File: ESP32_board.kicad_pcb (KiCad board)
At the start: 4 copper layers, 71 parts, among them J4 Conn_01x04_Pin, J5 Conn_01x05_Pin, Q2 BC817, Q3 BC817, U1 MCP73871, U5 USBLC6-2SC6

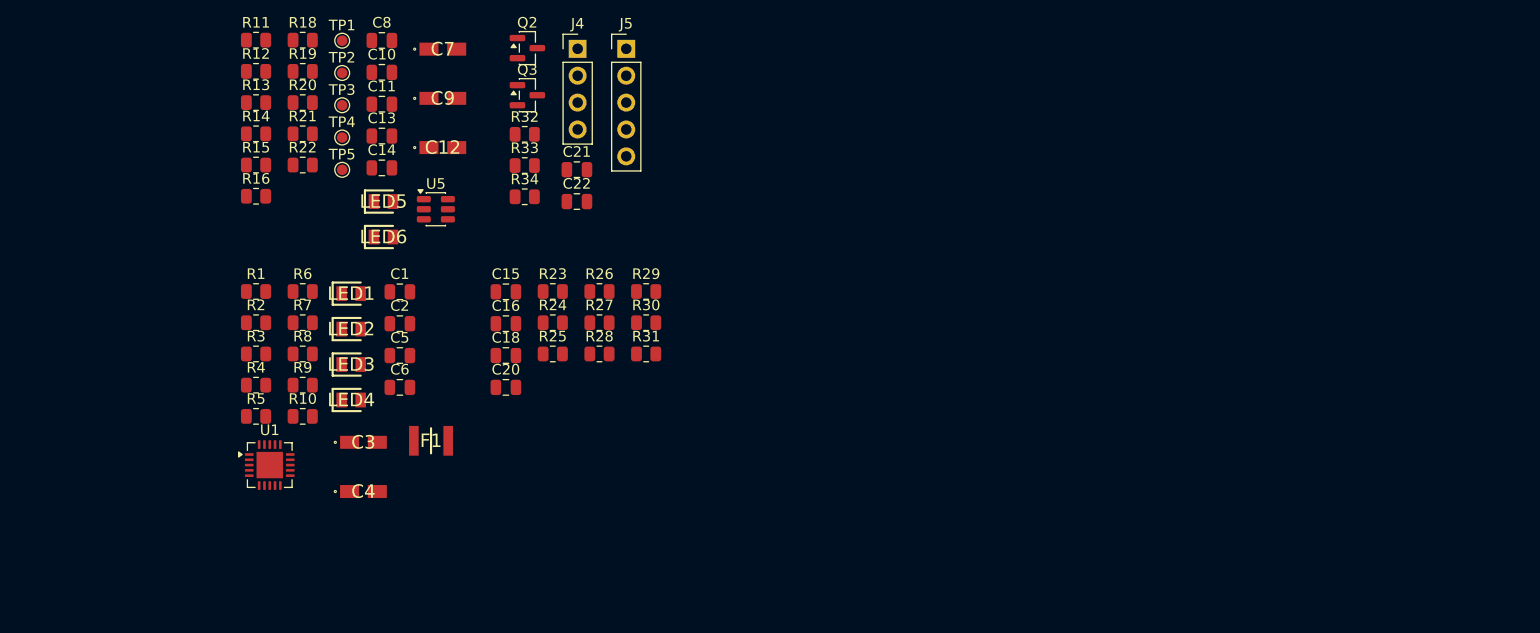
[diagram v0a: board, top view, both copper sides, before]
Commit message: imported all footprints into layout
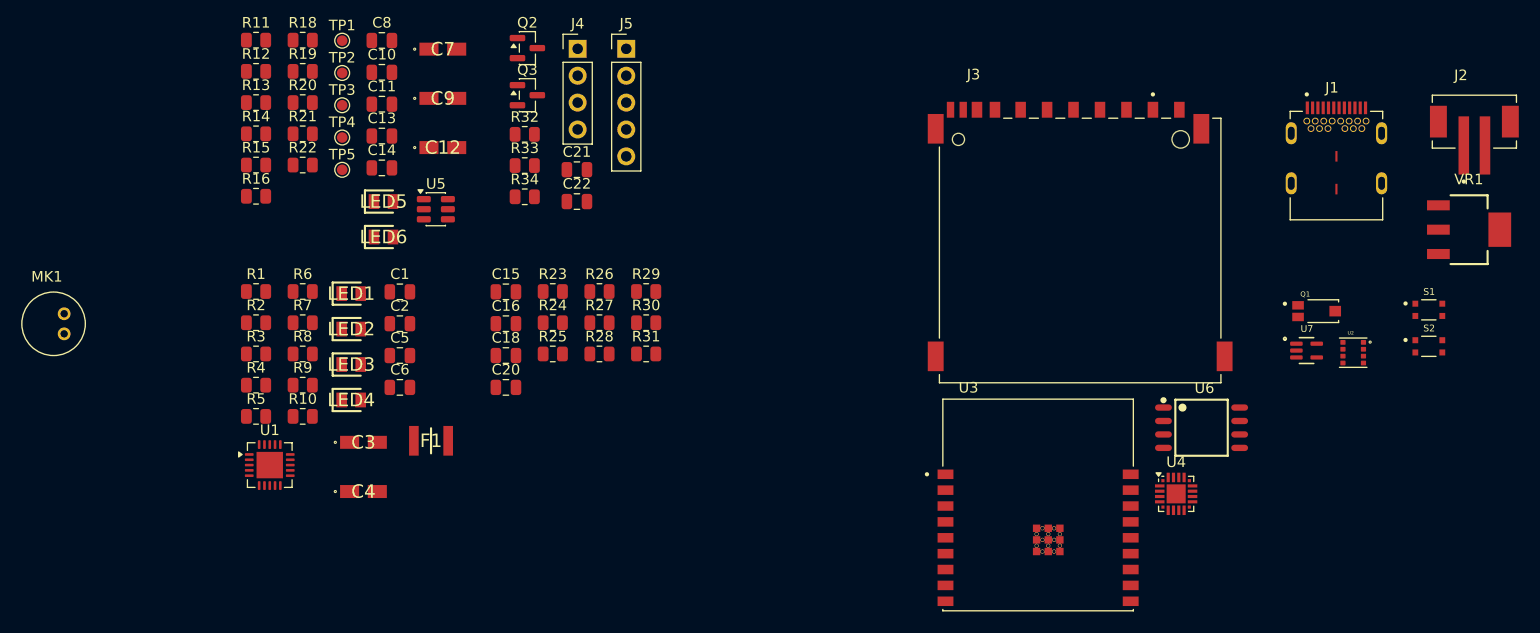
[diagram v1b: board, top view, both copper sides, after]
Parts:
- added J1: SS-52400-002, ESP32_project_Footprints:BELFUSE_SS-52400-002, F.Cu at (221.7, 59.4)
- added J2: B2B-PH-SM4-TB, ESP32_project_Footprints:JST_B2B-PH-SM4-TB, F.Cu at (234.7, 53.6)
- added J3: GSD090012SEU, ESP32_project_Footprints:AMPHENOL_GSD090012SEU, F.Cu at (197.5, 65.8)
- added MK1: CMC-5042PF-AC, ESP32_project_Footprints:CUI_CMC-5042PF-AC, F.Cu at (100.5, 72.7)
- added Q1: TEMT6000X01, ESP32_project_Footprints:TRANS_TEMT6000X01, F.Cu at (219.8, 71.5)
- added S1: Boot Button, ESP32_project_Footprints:SW_USLPT2819DT2TR, F.Cu at (230.4, 71.4)
- added S2: Reset Button, ESP32_project_Footprints:SW_USLPT2819DT2TR, F.Cu at (230.4, 74.8)
- added U2: BME280, ESP32_project_Footprints:PSON65P250X250X100-8N, F.Cu at (223.3, 75.4)
- added U3: ESP32-C3-WROOM-02-H4, ESP32_project_Footprints:MODULE_ESP32-C3-WROOM-02-H4, F.Cu at (193.5, 89.8)
- added U4: CP2102N-Axx-xQFN20, Package_DFN_QFN:SiliconLabs_QFN-20-1EP_3x3mm_P0.5mm_EP1.8x1.8mm, F.Cu at (206.5, 88.7)
- added U6: W25Q32JVSSIQ, ESP32_project_Footprints:SOIC127P790X216-8N, F.Cu at (208.9, 82.5)
- added U7: MAX4466EXK, ESP32_project_Footprints:SOT65P210X110-5N, F.Cu at (218.9, 75.2)
- added VR1: LM1117MPX-3.3, ESP32_project_Footprints:VREG_LM1117MPX-3.3, F.Cu at (234.2, 63.8)

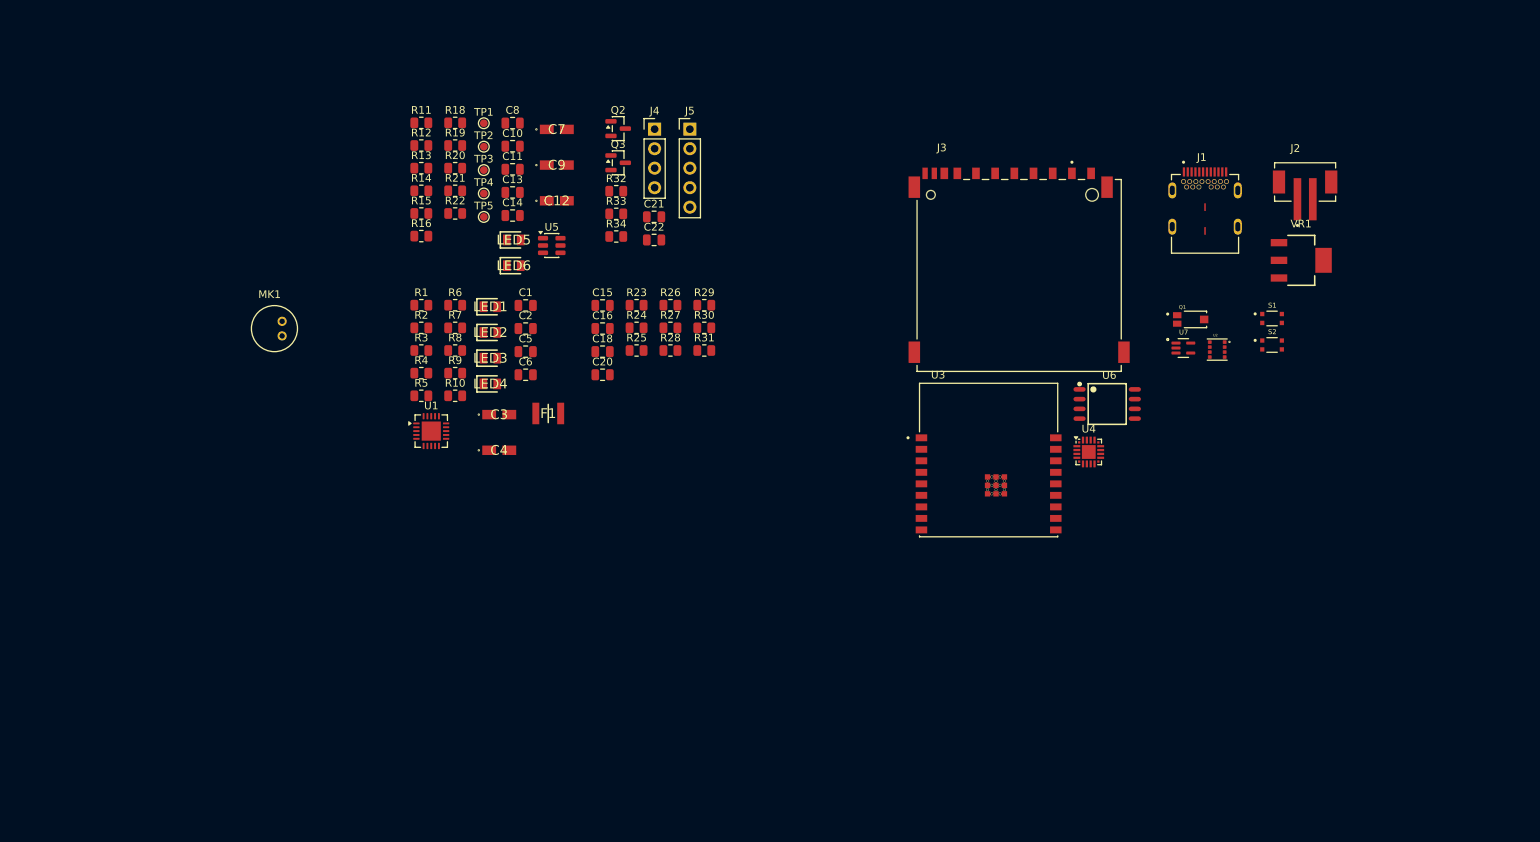
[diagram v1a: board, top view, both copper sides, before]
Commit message: finished rough layout placement
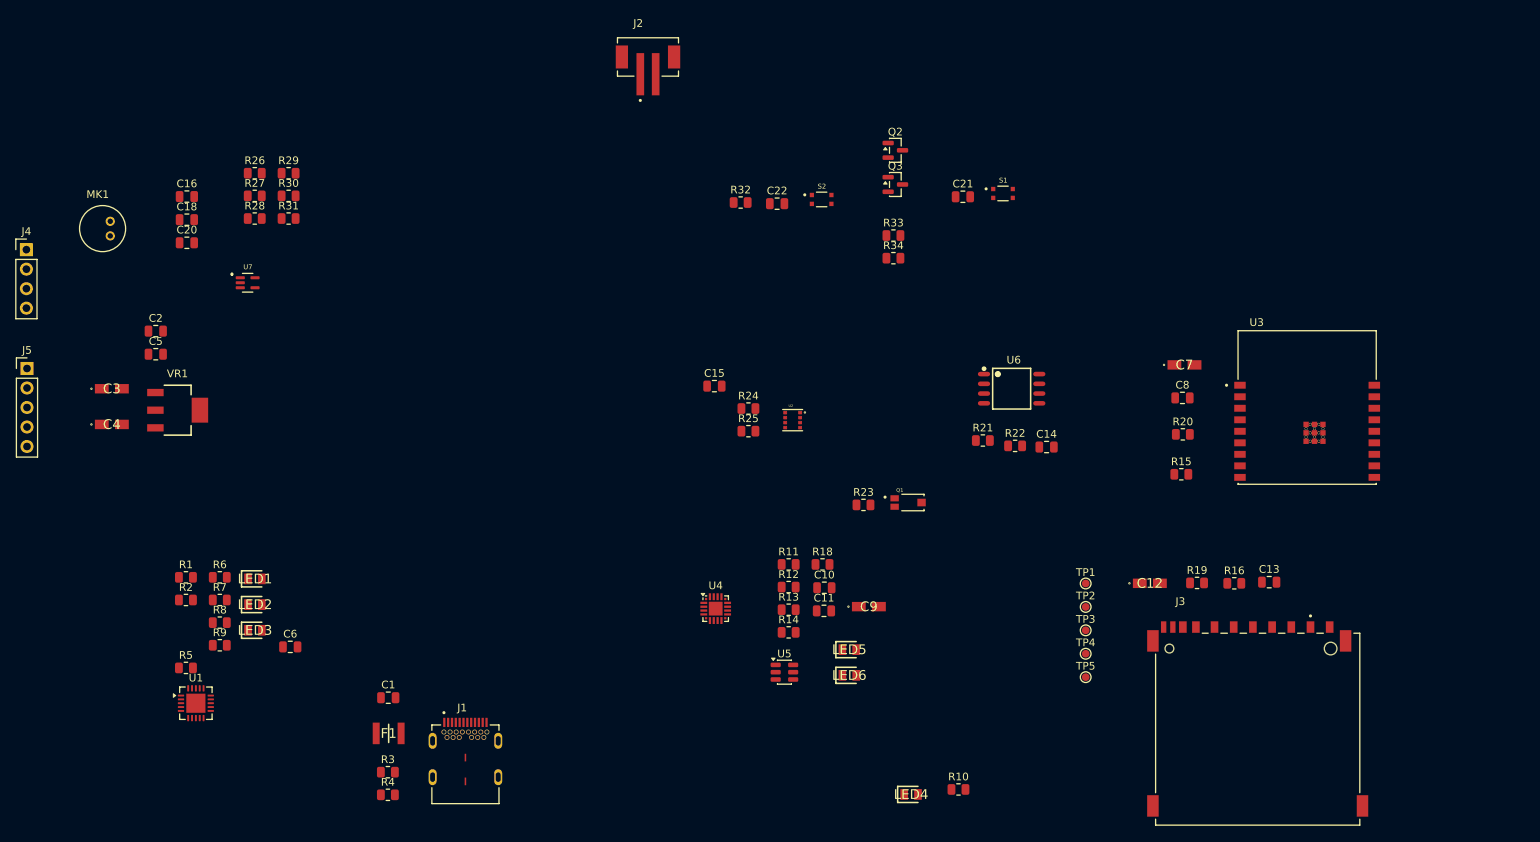
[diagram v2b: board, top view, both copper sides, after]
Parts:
- moved VR1 147.7 mm to (87.9, 83.3)
- moved U7 122.2 mm to (97.0, 66.7)
- moved J1 120.1 mm to (125.3, 131.1)
- moved R16 115.1 mm to (225.5, 105.8)
- moved R19 112.2 mm to (220.7, 105.8)
- moved C13 110.9 mm to (230.1, 105.7)
- moved R15 104.7 mm to (218.6, 91.7)
- moved R20 100.9 mm to (218.8, 86.5)
- moved TP1 98.7 mm to (206.1, 105.9)
- moved TP2 98.7 mm to (206.1, 108.9)
- moved TP3 98.7 mm to (206.1, 112.0)
- moved TP5 98.7 mm to (206.1, 118.1)
- moved TP4 98.7 mm to (206.1, 115.0)
- moved C8 94.3 mm to (218.8, 81.7)
- moved C12 91.9 mm to (214.5, 105.8)
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
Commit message: made edge cuts
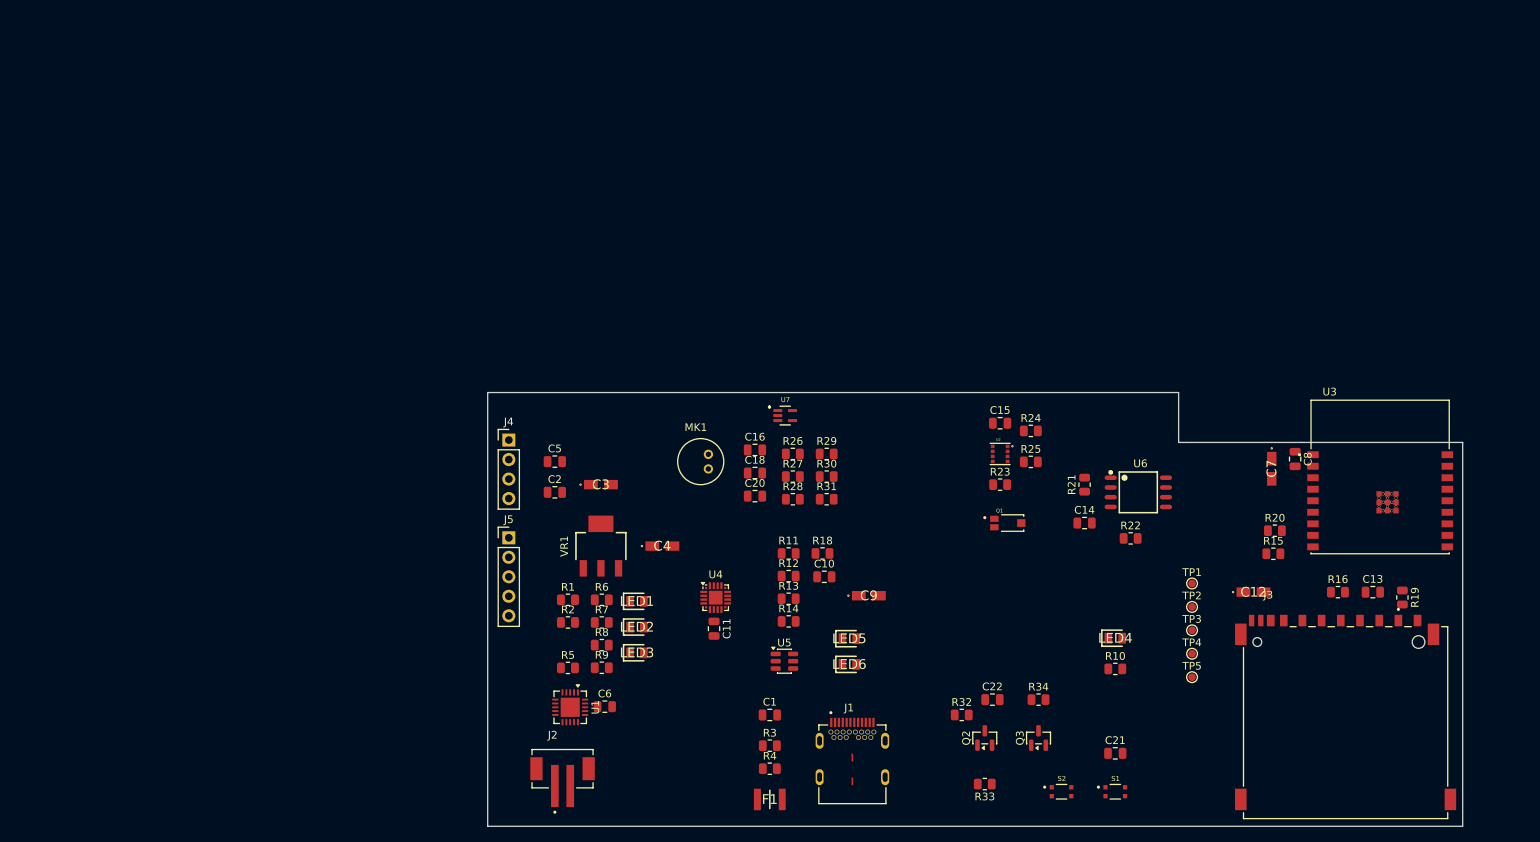
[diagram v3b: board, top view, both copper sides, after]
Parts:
- moved J2 93.4 mm to (138.0, 130.0)
- moved MK1 83.6 mm to (156.0, 90.0)
- moved S2 83.2 mm to (203.0, 133.0)
- moved C16 81.0 mm to (163.1, 88.5)
- moved C18 81.0 mm to (163.1, 91.5)
- moved C20 81.0 mm to (163.1, 94.5)
- moved S1 79.3 mm to (210.0, 133.0)
- moved R27 79.1 mm to (168.0, 92.0)
- moved R28 79.1 mm to (168.0, 94.9)
- moved R30 79.1 mm to (172.4, 92.0)
- moved R31 79.1 mm to (172.4, 94.9)
- moved R26 79.1 mm to (168.0, 89.0)
- moved R29 79.1 mm to (172.4, 89.0)
- moved Q2 77.4 mm to (193.0, 126.0), turned to 90 degrees
- moved C21 75.2 mm to (210.0, 128.0)
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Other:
- board outline added: 127 x 56.5 mm

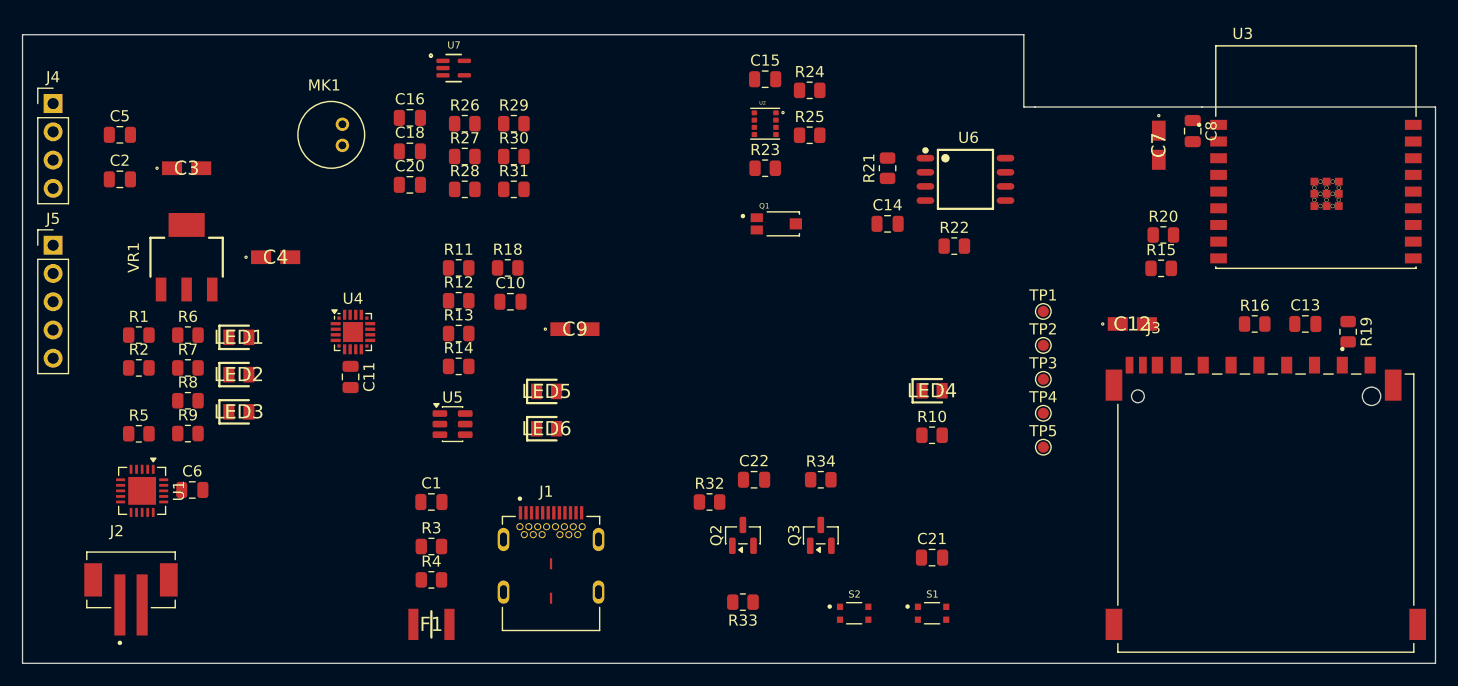
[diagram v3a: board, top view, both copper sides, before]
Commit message: finalized edge cuts and component placement
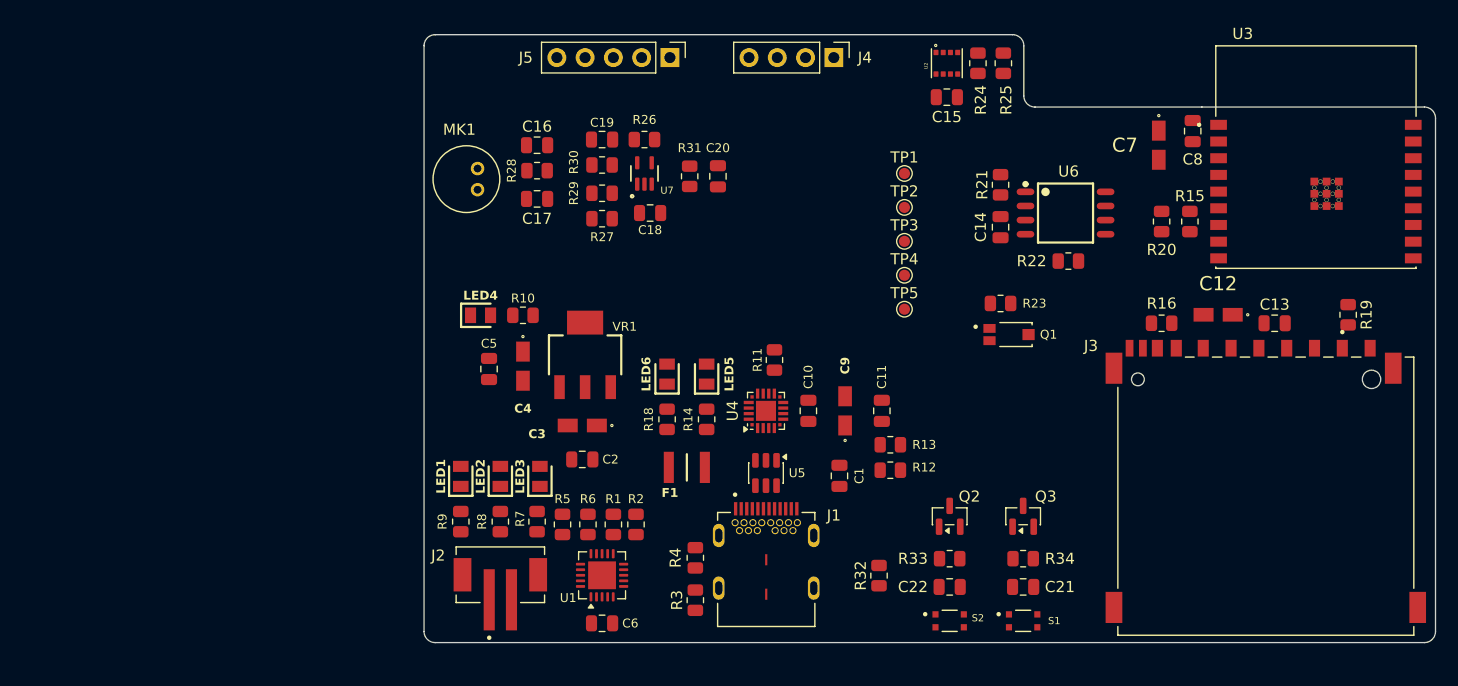
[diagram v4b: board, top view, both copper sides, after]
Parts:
- added C17: 0.01u, Capacitor_SMD:C_0805_2012Metric, F.Cu at (174.5, 95.8)
- added C19: 1u, Capacitor_SMD:C_0805_2012Metric, F.Cu at (180.3, 90.4)
- moved J4 70.3 mm to (201.2, 83.1), turned to -90 degrees
- moved J5 57.9 mm to (186.4, 83.1), turned to -90 degrees
- moved C2 48.6 mm to (178.6, 119.2), turned to 180 degrees
- moved C11 47.8 mm to (205.5, 114.8), turned to 90 degrees
- moved R2 46.8 mm to (183.4, 125.0), turned to 90 degrees
- moved R1 45.9 mm to (181.4, 125.0), turned to 90 degrees
- moved C3 42.4 mm to (178.6, 116.1), turned to 180 degrees
- moved U1 42.0 mm to (180.3, 129.6), turned to 90 degrees
- moved R12 41.7 mm to (206.2, 120.1), turned to 180 degrees
- moved LED4 41.1 mm to (169.4, 106.2)
- moved R13 40.1 mm to (206.2, 117.9)
- moved R6 39.8 mm to (179.1, 125.0), turned to 90 degrees
- moved C5 39.3 mm to (170.2, 111.0), turned to -90 degrees
- moved R5 38.9 mm to (176.8, 125.0), turned to 90 degrees
- moved C6 38.7 mm to (180.3, 133.9)
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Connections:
- net Net-(J1-CC1) renamed /CC1
- net Net-(J1-CC2) renamed /CC2
- net Net-(J3-DAT0) renamed /ESP32-C3-02/MISO_DO_SD
- net Net-(U3-IO6) renamed /ESP32-C3-02/SCLK_ESP32
- net Net-(U3-IO7) renamed /ESP32-C3-02/MOSI_DI_ESP32
- net Net-(U6-DO(IO1)) renamed /ESP32-C3-02/MISO_DO_FLASH
- net Net-(U7-IN-) renamed /ESP32-C3-02/Sensors/PREAMP_IN-
- MK1 pad OUT: Net-(U7-IN+) -> Net-(C17-Pad1)
- R27 pad 2: Net-(U7-IN+) -> /ESP32-C3-02/Sensors/PREAMP_IN+
- R28 pad 2: Net-(U7-IN+) -> Net-(C17-Pad1)
- R29 pad 1: Net-(U7-IN+) -> /ESP32-C3-02/Sensors/PREAMP_IN+
- R30 pad 2: GND -> Net-(C19-Pad2)
- U7 pad 1: Net-(U7-IN+) -> /ESP32-C3-02/Sensors/PREAMP_IN+
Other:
- board size 127 x 56.5 mm -> 90.9 x 54.6 mm
